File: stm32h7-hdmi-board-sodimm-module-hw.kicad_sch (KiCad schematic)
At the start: 0 parts

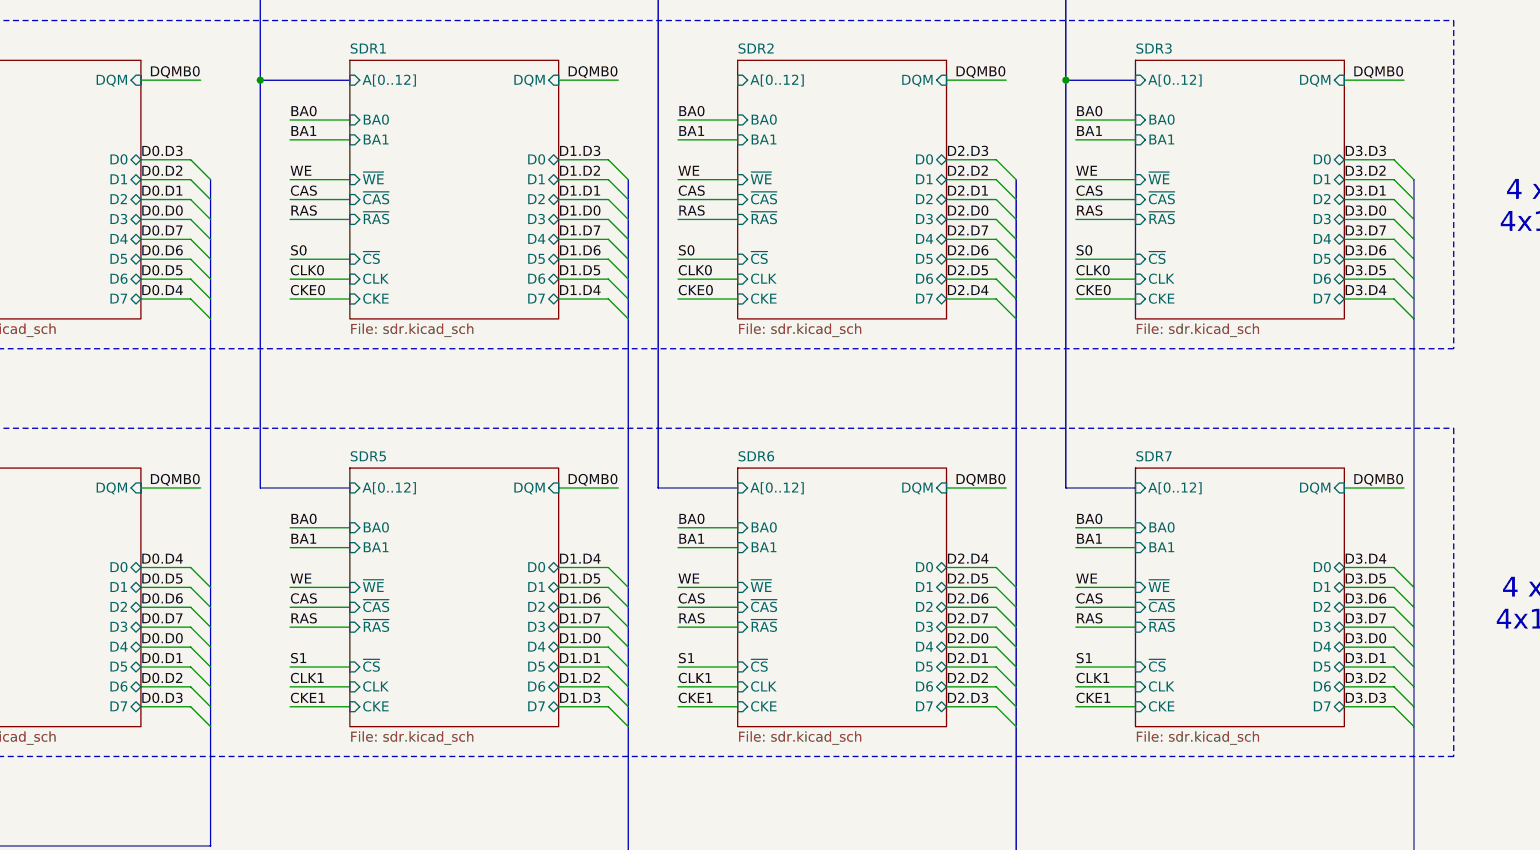
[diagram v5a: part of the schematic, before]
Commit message: [#100919] Reroute data bus, route clk0 and clk1
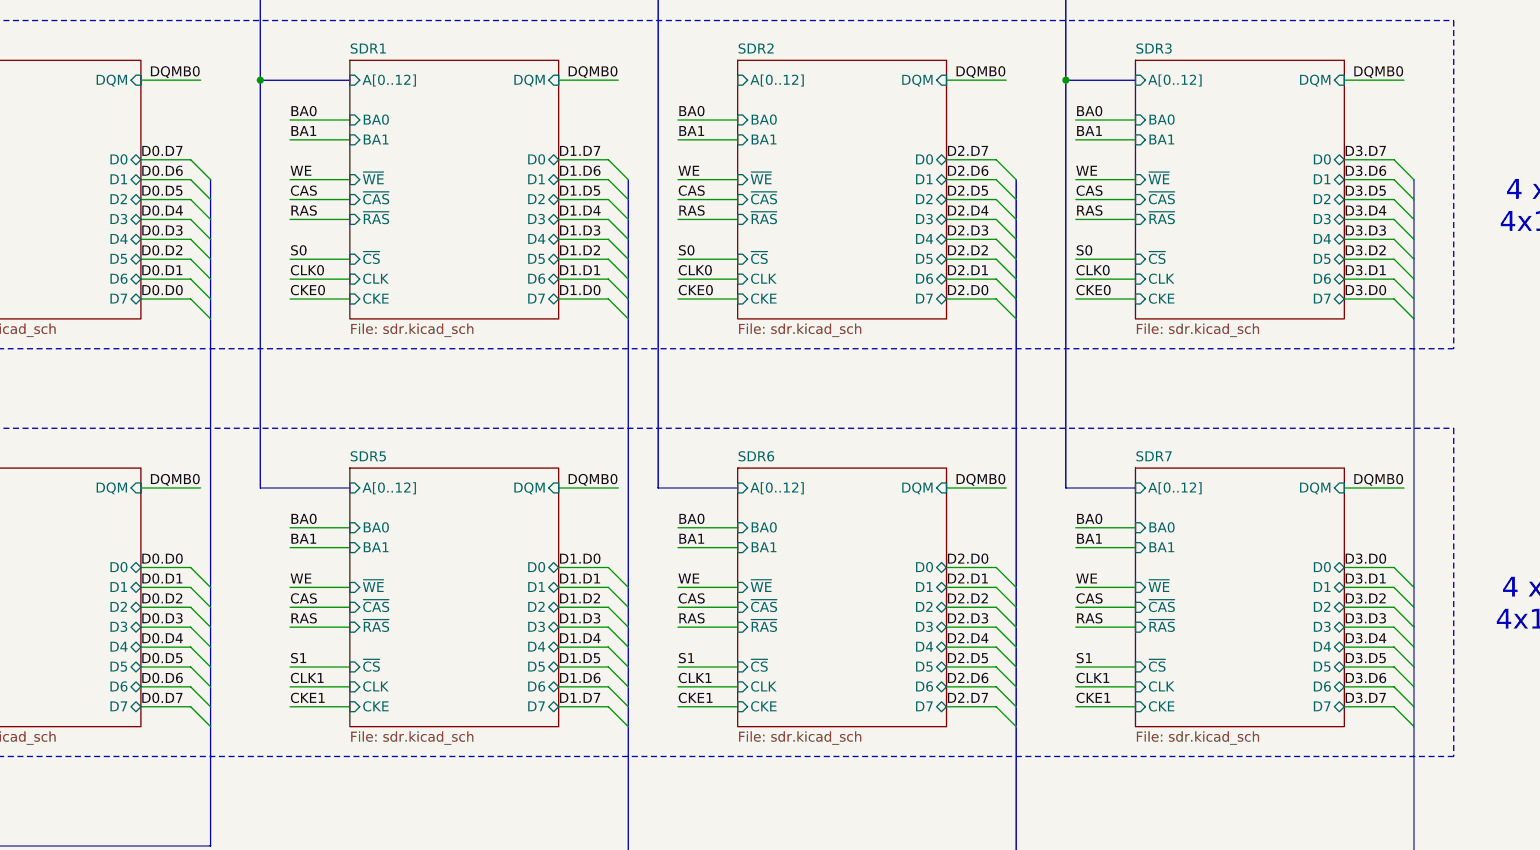
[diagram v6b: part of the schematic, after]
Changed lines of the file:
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@@
 	)
 	(label "D1.D6"
-		(at 229.87 107.95 0)
+		(at 229.87 97.79 0)
 		(effects
 			(font
@@
 	)
 	(label "D2.D2"
-		(at 279.4 97.79 0)
+		(at 279.4 107.95 0)
 		(effects
 			(font
@@
 	)
 	(label "D3.D2"
-		(at 330.2 162.56 0)
+		(at 330.2 152.4 0)
 		(effects
 			(font
@@
 	)
 	(label "D0.D6"
-		(at 176.53 152.4 0)
+		(at 176.53 162.56 0)
 		(effects
 			(font
@@
 	)
 	(label "D0.D5"
-		(at 176.53 110.49 0)
+		(at 176.53 100.33 0)
 		(effects
 			(font
@@
 	)
 	(label "D0.D6"
-		(at 176.53 107.95 0)
+		(at 176.53 97.79 0)
 		(effects
 			(font
@@
 	)
 	(label "D3.D1"
-		(at 330.2 100.33 0)
+		(at 330.2 110.49 0)
 		(effects
 			(font
@@
 	)
 	(label "D2.D3"
-		(at 279.4 165.1 0)
+		(at 279.4 154.94 0)
 		(effects
 			(font
@@
 	)
 	(label "D3.D5"
-		(at 330.2 149.86 0)
+		(at 330.2 160.02 0)
 		(effects
 			(font
@@
 	)
 	(label "D3.D0"
-		(at 330.2 157.48 0)
+		(at 330.2 147.32 0)
 		(effects
 			(font
@@
 	)
 	(label "D2.D2"
+		(at 279.4 152.4 0)
+		(effects
+			(font
+				(size 1.27 1.27)
+			)
+			(justify left bottom)
+		)
+	)
+	(label "D2.D6"
 		(at 279.4 162.56 0)
 		(effects
@@
 		)
 	)
-	(label "D2.D6"
-		(at 279.4 152.4 0)
-		(effects
-			(font
-				(size 1.27 1.27)
-			)
-			(justify left bottom)
-		)
-	)
 	(label "D0.D7"
-		(at 176.53 154.94 0)
+		(at 176.53 165.1 0)
 		(effects
 			(font
@@
 	)
 	(label "D2.D3"
-		(at 279.4 95.25 0)
+		(at 279.4 105.41 0)
 		(effects
 			(font
@@
 	)
 	(label "D3.D6"
-		(at 330.2 152.4 0)
+		(at 330.2 162.56 0)
 		(effects
 			(font
@@
 	)
 	(label "D1.D5"
-		(at 229.87 110.49 0)
+		(at 229.87 100.33 0)
 		(effects
 			(font
@@
 	)
 	(label "D2.D5"
-		(at 279.4 110.49 0)
+		(at 279.4 100.33 0)
 		(effects
 			(font
@@
 	)
 	(label "D1.D7"
-		(at 229.87 154.94 0)
+		(at 229.87 165.1 0)
 		(effects
 			(font
@@
 	)
 	(label "D2.D1"
-		(at 279.4 160.02 0)
+		(at 279.4 149.86 0)
 		(effects
 			(font
@@
 	)
 	(label "D0.D5"
-		(at 176.53 149.86 0)
+		(at 176.53 160.02 0)
 		(effects
 			(font
@@
 	)
 	(label "D1.D4"
-		(at 229.87 147.32 0)
+		(at 229.87 157.48 0)
 		(effects
 			(font
@@
 	)
 	(label "D3.D1"
-		(at 330.2 160.02 0)
+		(at 330.2 149.86 0)
 		(effects
 			(font
@@
 	)
 	(label "D0.D2"
-		(at 176.53 162.56 0)
+		(at 176.53 152.4 0)
 		(effects
 			(font
@@
 	)
 	(label "D2.D1"
-		(at 279.4 100.33 0)
+		(at 279.4 110.49 0)
 		(effects
 			(font
@@
 	)
 	(label "D0.D2"
-		(at 176.53 97.79 0)
+		(at 176.53 107.95 0)
 		(effects
 			(font
@@
 	)
 	(label "D0.D7"
-		(at 176.53 105.41 0)
+		(at 176.53 95.25 0)
 		(effects
 			(font
@@
 	)
 	(label "D1.D3"
-		(at 229.87 95.25 0)
+		(at 229.87 105.41 0)
 		(effects
 			(font
@@
 	)
 	(label "D0.D3"
-		(at 176.53 95.25 0)
+		(at 176.53 105.41 0)
 		(effects
 			(font
@@
 	)
 	(label "D1.D0"
-		(at 229.87 157.48 0)
+		(at 229.87 147.32 0)
 		(effects
 			(font
@@
 	)
 	(label "D3.D4"
-		(at 330.2 113.03 0)
+		(at 330.2 102.87 0)
 		(effects
 			(font
@@
 	)
 	(label "D3.D7"
-		(at 330.2 105.41 0)
+		(at 330.2 95.25 0)
 		(effects
 			(font
@@
 	)
 	(label "D2.D0"
-		(at 279.4 102.87 0)
+		(at 279.4 113.03 0)
 		(effects
 			(font
@@
 	)
 	(label "D1.D5"
-		(at 229.87 149.86 0)
+		(at 229.87 160.02 0)
 		(effects
 			(font
@@
 	)
 	(label "D1.D6"
-		(at 229.87 152.4 0)
+		(at 229.87 162.56 0)
 		(effects
 			(font
@@
 	)
 	(label "D3.D0"
-		(at 330.2 102.87 0)
+		(at 330.2 113.03 0)
 		(effects
 			(font
@@
 	)
 	(label "D0.D1"
-		(at 176.53 160.02 0)
+		(at 176.53 149.86 0)
 		(effects
 			(font
@@
 	)
 	(label "D3.D2"
-		(at 330.2 97.79 0)
+		(at 330.2 107.95 0)
 		(effects
 			(font
@@
 	)
 	(label "D1.D1"
-		(at 229.87 160.02 0)
+		(at 229.87 149.86 0)
 		(effects
 			(font
@@
 	)
 	(label "D2.D4"
-		(at 279.4 147.32 0)
+		(at 279.4 157.48 0)
 		(effects
 			(font
@@
 	)
 	(label "D1.D3"
-		(at 229.87 165.1 0)
+		(at 229.87 154.94 0)
 		(effects
 			(font
@@
 	)
 	(label "D0.D4"
-		(at 176.53 147.32 0)
+		(at 176.53 157.48 0)
 		(effects
 			(font
@@
 	)
 	(label "D1.D7"
-		(at 229.87 105.41 0)
+		(at 229.87 95.25 0)
 		(effects
 			(font
@@
 	)
 	(label "D2.D7"
-		(at 279.4 105.41 0)
+		(at 279.4 95.25 0)
 		(effects
 			(font
@@
 	)
 	(label "D1.D0"
-		(at 229.87 102.87 0)
+		(at 229.87 113.03 0)
 		(effects
 			(font
@@
 	)
 	(label "D2.D7"
-		(at 279.4 154.94 0)
+		(at 279.4 165.1 0)
 		(effects
 			(font
@@
 	)
 	(label "D1.D2"
-		(at 229.87 162.56 0)
+		(at 229.87 152.4 0)
 		(effects
 			(font
@@
 	)
 	(label "D3.D7"
-		(at 330.2 154.94 0)
+		(at 330.2 165.1 0)
 		(effects
 			(font
@@
 	)
 	(label "D2.D6"
-		(at 279.4 107.95 0)
+		(at 279.4 97.79 0)
 		(effects
 			(font
@@
 	)
 	(label "D3.D5"
-		(at 330.2 110.49 0)
+		(at 330.2 100.33 0)
 		(effects
 			(font
@@
 	)
 	(label "D0.D0"
-		(at 176.53 157.48 0)
+		(at 176.53 147.32 0)
 		(effects
 			(font
@@
 	)
 	(label "D3.D4"
-		(at 330.2 147.32 0)
+		(at 330.2 157.48 0)
 		(effects
 			(font
@@
 	)
 	(label "D2.D5"
-		(at 279.4 149.86 0)
+		(at 279.4 160.02 0)
 		(effects
 			(font
@@
 	)
 	(label "D0.D0"
-		(at 176.53 102.87 0)
+		(at 176.53 113.03 0)
 		(effects
 			(font
@@
 	)
 	(label "D1.D1"
-		(at 229.87 100.33 0)
+		(at 229.87 110.49 0)
 		(effects
 			(font
@@
 	)
 	(label "D2.D0"
-		(at 279.4 157.48 0)
+		(at 279.4 147.32 0)
 		(effects
 			(font
@@
 	)
 	(label "D1.D2"
-		(at 229.87 97.79 0)
+		(at 229.87 107.95 0)
 		(effects
 			(font
@@
 	)
 	(label "D3.D6"
-		(at 330.2 107.95 0)
+		(at 330.2 97.79 0)
 		(effects
 			(font
@@
 	)
 	(label "D0.D1"
-		(at 176.53 100.33 0)
+		(at 176.53 110.49 0)
 		(effects
 			(font
@@
 	)
 	(label "D0.D3"
-		(at 176.53 165.1 0)
+		(at 176.53 154.94 0)
 		(effects
 			(font
@@
 	)
 	(label "D3.D3"
-		(at 330.2 95.25 0)
+		(at 330.2 105.41 0)
 		(effects
 			(font
@@
 	)
 	(label "D0.D4"
-		(at 176.53 113.03 0)
+		(at 176.53 102.87 0)
 		(effects
 			(font
@@
 	)
 	(label "D1.D4"
-		(at 229.87 113.03 0)
+		(at 229.87 102.87 0)
 		(effects
 			(font
@@
 	)
 	(label "D3.D3"
-		(at 330.2 165.1 0)
+		(at 330.2 154.94 0)
 		(effects
 			(font
@@
 	)
 	(label "D2.D4"
-		(at 279.4 113.03 0)
-		(effects
-			(font
+		(at 279.4 102.87 0)
+		(effects
+			(font

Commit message: [#100919] Schematic update
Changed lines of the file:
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@@
 	)
 	(junction
+		(at 242.57 85.09)
+		(diameter 0)
+		(color 0 0 0 0)
+	)
+	(junction
 		(at 242.57 63.5)
 		(diameter 0)
@@
 		)
 	)
+	(bus
+		(pts
+			(xy 242.57 85.09) (xy 252.73 85.09)
+		)
+		(stroke
+			(width 0)
+			(type default)
+		)
+	)
 	(wire
 		(pts
@@
 	(bus
 		(pts
-			(xy 242.57 63.5) (xy 242.57 137.16)
+			(xy 242.57 63.5) (xy 242.57 85.09)
 		)
 		(stroke
@@
 		)
 	)
+	(bus
+		(pts
+			(xy 242.57 85.09) (xy 242.57 137.16)
+		)
+		(stroke
+			(width 0)
+			(type default)
+		)
+	)
 	(wire
 		(pts
@@
 		)
 	)
-	(label "DQMB0"
+	(label "DQMB2"
 		(at 287.02 137.16 180)
 		(effects
@@
 		)
 	)
-	(label "DQMB0"
+	(label "DQMB3"
 		(at 337.82 137.16 180)
 		(effects
@@
 		)
 	)
-	(label "DQMB0"
+	(label "DQMB1"
 		(at 237.49 137.16 180)
 		(effects
@@
 		)
 	)
-	(label "DQMB0"
+	(label "DQMB2"
 		(at 287.02 85.09 180)
 		(effects
@@
 		)
 	)
-	(label "DQMB0"
+	(label "DQMB1"
 		(at 237.49 85.09 180)
 		(effects
@@
 		)
 	)
-	(label "DQMB0"
+	(label "DQMB3"
 		(at 337.82 85.09 180)
 		(effects

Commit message: [#101386] Add logo
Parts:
- added N1: antmicro_logo, antmicro-footprints:antmicro-logo_scaled_12mm, symbol antmicroMechanicalParts:antmicro_logo
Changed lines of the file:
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@@
+		)
+	)
+	(symbol
+		(lib_id "antmicroMechanicalParts:antmicro_logo")
+		(at 36.83 186.69 0)
+		(unit 1)
+		(body_style 1)
+		(exclude_from_sim no)
+		(in_bom no)
+		(on_board yes)
+		(in_pos_files yes)
+		(dnp no)
+		(fields_autoplaced yes)
+		(property "Reference" "N1"
+			(at 43.18 184.7062 0)
+			(show_name no)
+			(do_not_autoplace no)
+			(effects
+				(font
+					(size 1.27 1.27)
+					(thickness 0.15)
+				)
+				(justify left)
+			)
+		)
+		(property "Value" "antmicro_logo"
+			(at 43.18 187.2462 0)
+			(show_name no)
+			(do_not_autoplace no)
+			(effects
+				(font
+					(size 1.27 1.27)
+					(thickness 0.15)
+				)
+				(justify left)
+			)
+		)
+		(property "Footprint" "antmicro-footprints:antmicro-logo_scaled_12mm"
+			(at 52.07 196.85 0)
+			(hide yes)
+			(show_name no)
+			(do_not_autoplace no)
+			(effects
+				(font
+					(size 1.27 1.27)
+					(thickness 0.15)
+				)
+				(justify left bottom)
+			)
+		)
+		(property "Datasheet" ""
+			(at 52.07 199.39 0)
+			(hide yes)
+			(show_name no)
+			(do_not_autoplace no)
+			(effects
+				(font
+					(size 1.27 1.27)
+					(thickness 0.15)
+				)
+				(justify left bottom)
+			)
+		)
+		(property "Description" "Mechanical part"
+			(at 52.07 209.55 0)
+			(hide yes)
+			(show_name no)
+			(do_not_autoplace no)
+			(effects
+				(font
+					(size 1.27 1.27)
+				)
+				(justify left bottom)
+			)
+		)
+		(property "MPN" ""
+			(at 36.83 186.69 0)
+			(show_name no)
+			(do_not_autoplace no)
+			(effects
+				(font
+					(size 1.27 1.27)
+				)
+			)
+		)
+		(property "Manufacturer" ""
+			(at 52.07 207.01 0)
+			(hide yes)
+			(show_name no)
+			(do_not_autoplace no)
+			(effects
+				(font
+					(size 1.27 1.27)
+					(thickness 0.15)
+				)
+				(justify left bottom)
+			)
+		)
+		(property "Author" "Antmicro"
+			(at 52.07 201.93 0)
+			(hide yes)
+			(show_name no)
+			(do_not_autoplace no)
+			(effects
+				(font
+					(size 1.27 1.27)
+					(thickness 0.15)
+				)
+				(justify left bottom)
+			)
+		)
+		(property "License" "Apache-2.0"
+			(at 52.07 204.47 0)
+			(hide yes)
+			(show_name no)
+			(do_not_autoplace no)
+			(effects
+				(font
+					(size 1.27 1.27)
+					(thickness 0.15)
+				)
+				(justify left bottom)
+			)
+		)
+		(instances
+			(project "stm32h7-hdmi-board-sodimm-module-hw"
+				(path "/92fcd7c5-798f-49cd-ae80-ce2fa78a6354"
+					(reference "N1")
+					(unit 1)
+				)
+			)
 		)
 	)
